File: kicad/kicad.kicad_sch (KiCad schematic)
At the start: 32 parts, among them J1 12V_INPUT, J2 MOTOR_OUT, J3 NUCLEO_HEADER, J4 CAN_BUS, Q1 IRLZ44NPBF, U1 TC4427ACPA, U2 INA180A1IDBVR, U3 TCAN332DR

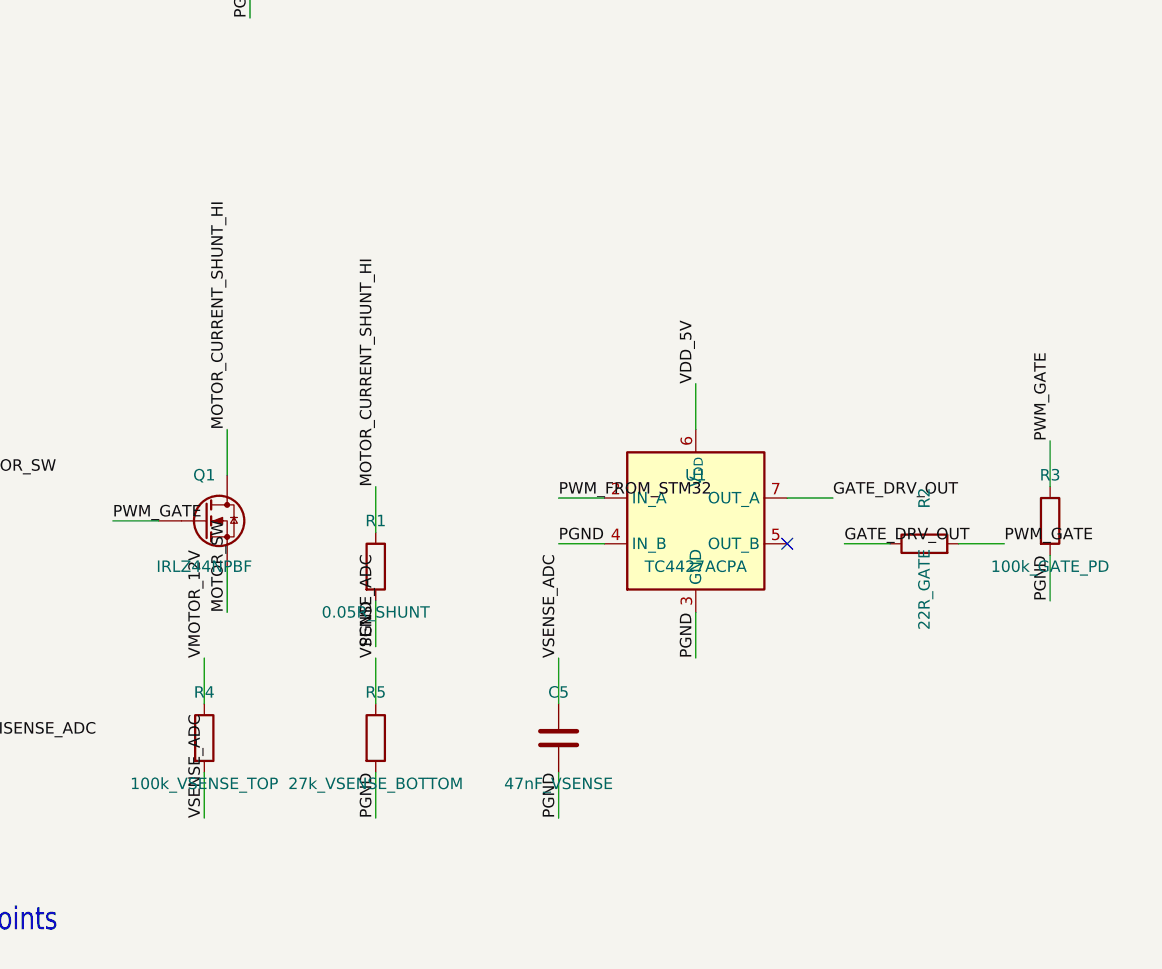
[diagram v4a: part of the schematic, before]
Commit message: Prepare PCB placement without routing
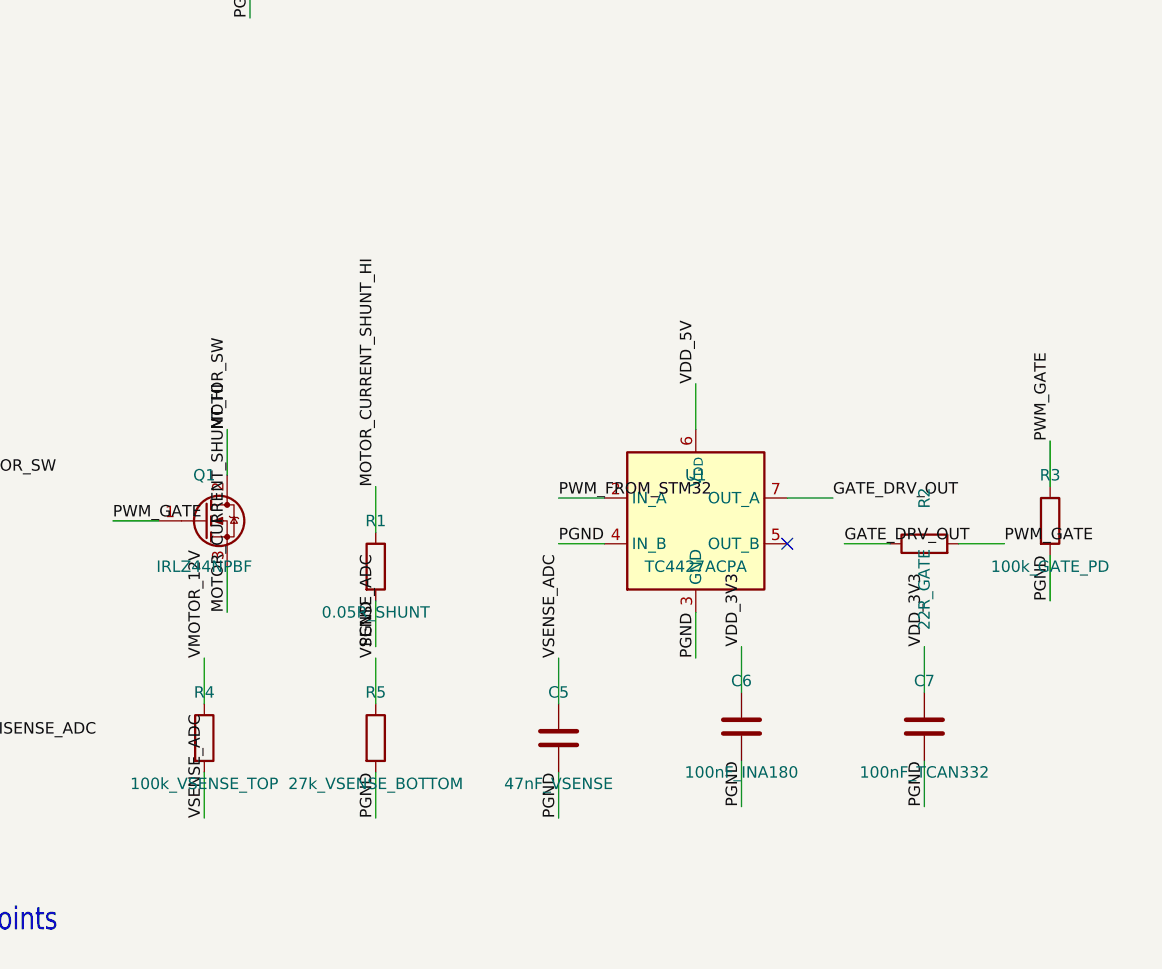
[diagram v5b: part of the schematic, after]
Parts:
- added C6: 100nF_INA180, Capacitor_SMD:C_0805_2012Metric, symbol Device:C
- added C7: 100nF_TCAN332, Capacitor_SMD:C_0805_2012Metric, symbol Device:C
- F1: footprint Fuse:Fuseholder_Clip-5x20mm_Littelfuse_111_Inline_P20.00x5.00mm_D1.05mm_Horizontal -> Project_Footprints:Littelfuse_RXEF110
- J1, J2: footprint TerminalBlock:TerminalBlock_MaiXu_MX126-5.0-02P_1x02_P5.00mm -> Project_Footprints:OnShore_OSTVN02A150
- J4: footprint TerminalBlock:TerminalBlock_MaiXu_MX126-5.0-03P_1x03_P5.00mm -> Project_Footprints:OnShore_OSTVN03A150
- Q1: symbol Device:Q_NMOS -> Transistor_FET:IRLIZ44N
- TH1: footprint Resistor_SMD:R_0805_2012Metric -> Resistor_THT:R_Axial_DIN0204_L3.6mm_D1.6mm_P2.54mm_Vertical
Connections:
- net MOTOR_CURRENT_SHUNT_HI: now also Q1.3 (S); no longer Q1.D
- net MOTOR_SW: now also Q1.2 (D); no longer Q1.S
- net PGND: now also C6.2, C7.2
- net PWM_GATE: now also Q1.1 (G); no longer Q1.G
- net VDD_3V3: now also C6.1, C7.1
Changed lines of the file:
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@@
 		(property "Reference" "J1" (at 35.56 30.48 0) (effects (font (size 1.27 1.27))))
 		(property "Value" "12V_INPUT" (at 35.56 39.37 0) (effects (font (size 1.27 1.27))))
-		(property "Footprint" "TerminalBlock:TerminalBlock_MaiXu_MX126-5.0-02P_1x02_P5.00mm" (at 35.56 35.56 0) (effects (font (size 1.27 1.27)) (hide yes)))
+		(property "Footprint" "Project_Footprints:OnShore_OSTVN02A150" (at 35.56 35.56 0) (effects (font (size 1.27 1.27)) (hide yes)))
 		(property "Datasheet" "" (at 35.56 35.56 0) (effects (font (size 1.27 1.27)) (hide yes)))
 		(instances (project "kicad" (path "/" (reference "J1") (unit 1))))
@@
 		(property "Reference" "F1" (at 59.69 30.48 0) (effects (font (size 1.27 1.27))))
 		(property "Value" "RXEF110_PTC" (at 59.69 39.37 0) (effects (font (size 1.27 1.27))))
-		(property "Footprint" "Fuse:Fuseholder_Clip-5x20mm_Littelfuse_111_Inline_P20.00x5.00mm_D1.05mm_Horizontal" (at 59.69 35.56 0) (effects (font (size 1.27 1.27)) (hide yes)))
+		(property "Footprint" "Project_Footprints:Littelfuse_RXEF110" (at 59.69 35.56 0) (effects (font (size 1.27 1.27)) (hide yes)))
 		(property "Datasheet" "" (at 59.69 35.56 0) (effects (font (size 1.27 1.27)) (hide yes)))
 		(instances (project "kicad" (path "/" (reference "F1") (unit 1))))
@@
 		(property "Reference" "J2" (at 35.56 90.17 0) (effects (font (size 1.27 1.27))))
 		(property "Value" "MOTOR_OUT" (at 35.56 100.33 0) (effects (font (size 1.27 1.27))))
-		(property "Footprint" "TerminalBlock:TerminalBlock_MaiXu_MX126-5.0-02P_1x02_P5.00mm" (at 35.56 95.25 0) (effects (font (size 1.27 1.27)) (hide yes)))
+		(property "Footprint" "Project_Footprints:OnShore_OSTVN02A150" (at 35.56 95.25 0) (effects (font (size 1.27 1.27)) (hide yes)))
 		(property "Datasheet" "" (at 35.56 95.25 0) (effects (font (size 1.27 1.27)) (hide yes)))
 		(instances (project "kicad" (path "/" (reference "J2") (unit 1))))
@@
 	(wire (pts (xy 73.66 95.25) (xy 78.74 95.25)) (stroke (width 0) (type solid)))
 	(label "MOTOR_SW" (at 78.74 95.25 0) (effects (font (size 1.27 1.27)) (justify left bottom)))
-	(symbol (lib_id "Device:Q_NMOS") (at 105.41 100.33 0) (unit 1) (exclude_from_sim no) (in_bom yes) (on_board yes) (dnp no)
+	(symbol (lib_id "Transistor_FET:IRLIZ44N") (at 105.41 100.33 0) (unit 1) (exclude_from_sim no) (in_bom yes) (on_board yes) (dnp no)
 		(property "Reference" "Q1" (at 105.41 95.25 0) (effects (font (size 1.27 1.27))))
 		(property "Value" "IRLZ44NPBF" (at 105.41 105.41 0) (effects (font (size 1.27 1.27))))
@@
 	)
 	(wire (pts (xy 107.95 105.41) (xy 107.95 110.49)) (stroke (width 0) (type solid)))
-	(label "MOTOR_SW" (at 107.95 110.49 270) (effects (font (size 1.27 1.27)) (justify left bottom)))
+	(label "MOTOR_CURRENT_SHUNT_HI" (at 107.95 110.49 270) (effects (font (size 1.27 1.27)) (justify left bottom)))
 	(wire (pts (xy 100.33 100.33) (xy 95.25 100.33)) (stroke (width 0) (type solid)))
 	(label "PWM_GATE" (at 95.25 100.33 180) (effects (font (size 1.27 1.27)) (justify left bottom)))
 	(wire (pts (xy 107.95 95.25) (xy 107.95 90.17)) (stroke (width 0) (type solid)))
-	(label "MOTOR_CURRENT_SHUNT_HI" (at 107.95 90.17 90) (effects (font (size 1.27 1.27)) (justify left bottom)))
+	(label "MOTOR_SW" (at 107.95 90.17 90) (effects (font (size 1.27 1.27)) (justify left bottom)))
 	(symbol (lib_id "Device:R") (at 124.46 105.41 0) (unit 1) (exclude_from_sim no) (in_bom yes) (on_board yes) (dnp no)
 		(property "Reference" "R1" (at 124.46 100.33 0) (effects (font (size 1.27 1.27))))
@@
 	(wire (pts (xy 144.78 128.27) (xy 144.78 133.35)) (stroke (width 0) (type solid)))
 	(label "PGND" (at 144.78 133.35 270) (effects (font (size 1.27 1.27)) (justify left bottom)))
-	(symbol (lib_id "Connector_Generic:Conn_01x09") (at 54.61 180.34 0) (unit 1) (exclude_from_sim no) (in_bom yes) (on_board yes) (dnp no)
+		(symbol (lib_id "Device:C") (at 165.1 123.19 0) (unit 1) (exclude_from_sim no) (in_bom yes) (on_board yes) (dnp no)
+		(property "Reference" "C6" (at 165.1 118.11 0) (effects (font (size 1.27 1.27))))
+		(property "Value" "100nF_INA180" (at 165.1 128.27 0) (effects (font (size 1.27 1.27))))
+		(property "Footprint" "Capacitor_SMD:C_0805_2012Metric" (at 165.1 123.19 0) (effects (font (size 1.27 1.27)) (hide yes)))
+		(property "Datasheet" "" (at 165.1 123.19 0) (effects (font (size 1.27 1.27)) (hide yes)))
+		(instances (project "kicad" (path "/" (reference "C6") (unit 1))))
+	)
+	(wire (pts (xy 165.1 119.38) (xy 165.1 114.3)) (stroke (width 0) (type solid)))
+	(label "VDD_3V3" (at 165.1 114.3 90) (effects (font (size 1.27 1.27)) (justify left bottom)))
+	(wire (pts (xy 165.1 127.0) (xy 165.1 132.08)) (stroke (width 0) (type solid)))
+	(label "PGND" (at 165.1 132.08 270) (effects (font (size 1.27 1.27)) (justify left bottom)))
+	(symbol (lib_id "Device:C") (at 185.42 123.19 0) (unit 1) (exclude_from_sim no) (in_bom yes) (on_board yes) (dnp no)
+		(property "Reference" "C7" (at 185.42 118.11 0) (effects (font (size 1.27 1.27))))
+		(property "Value" "100nF_TCAN332" (at 185.42 128.27 0) (effects (font (size 1.27 1.27))))
+		(property "Footprint" "Capacitor_SMD:C_0805_2012Metric" (at 185.42 123.19 0) (effects (font (size 1.27 1.27)) (hide yes)))
+		(property "Datasheet" "" (at 185.42 123.19 0) (effects (font (size 1.27 1.27)) (hide yes)))
+		(instances (project "kicad" (path "/" (reference "C7") (unit 1))))
+	)
+	(wire (pts (xy 185.42 119.38) (xy 185.42 114.3)) (stroke (width 0) (type solid)))
+	(label "VDD_3V3" (at 185.42 114.3 90) (effects (font (size 1.27 1.27)) (justify left bottom)))
+	(wire (pts (xy 185.42 127.0) (xy 185.42 132.08)) (stroke (width 0) (type solid)))
+	(label "PGND" (at 185.42 132.08 270) (effects (font (size 1.27 1.27)) (justify left bottom)))(symbol (lib_id "Connector_Generic:Conn_01x09") (at 54.61 180.34 0) (unit 1) (exclude_from_sim no) (in_bom yes) (on_board yes) (dnp no)
 		(property "Reference" "J3" (at 54.61 175.26 0) (effects (font (size 1.27 1.27))))
 		(property "Value" "NUCLEO_HEADER" (at 54.61 185.42 0) (effects (font (size 1.27 1.27))))
@@
 		(property "Reference" "TH1" (at 110.49 175.26 0) (effects (font (size 1.27 1.27))))
 		(property "Value" "10k_NTC" (at 110.49 185.42 0) (effects (font (size 1.27 1.27))))
-		(property "Footprint" "Resistor_SMD:R_0805_2012Metric" (at 110.49 180.34 0) (effects (font (size 1.27 1.27)) (hide yes)))
+		(property "Footprint" "Resistor_THT:R_Axial_DIN0204_L3.6mm_D1.6mm_P2.54mm_Vertical" (at 110.49 180.34 0) (effects (font (size 1.27 1.27)) (hide yes)))
 		(property "Datasheet" "" (at 110.49 180.34 0) (effects (font (size 1.27 1.27)) (hide yes)))
 		(instances (project "kicad" (path "/" (reference "TH1") (unit 1))))
@@
 		(property "Reference" "J4" (at 219.71 175.26 0) (effects (font (size 1.27 1.27))))
 		(property "Value" "CAN_BUS" (at 219.71 185.42 0) (effects (font (size 1.27 1.27))))
-		(property "Footprint" "TerminalBlock:TerminalBlock_MaiXu_MX126-5.0-03P_1x03_P5.00mm" (at 219.71 180.34 0) (effects (font (size 1.27 1.27)) (hide yes)))
+		(property "Footprint" "Project_Footprints:OnShore_OSTVN03A150" (at 219.71 180.34 0) (effects (font (size 1.27 1.27)) (hide yes)))
 		(property "Datasheet" "" (at 219.71 180.34 0) (effects (font (size 1.27 1.27)) (hide yes)))
 		(instances (project "kicad" (path "/" (reference "J4") (unit 1))))
